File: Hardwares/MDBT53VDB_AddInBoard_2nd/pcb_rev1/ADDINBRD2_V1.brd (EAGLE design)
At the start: 25 x 31 mm, 21 parts, among them CN1 IF_4PIN, CN2 IF_4PIN, CN3 IF_2PIN, CN4 IF_2PIN, Q1 DMP2035UFDF-7, Q2 BC817-40QA, SW1 SKRPACE010, U1 SN74AHC1G00DRLR, U2 REF3325AIRSER, U3 MCP6232T-E/MNY

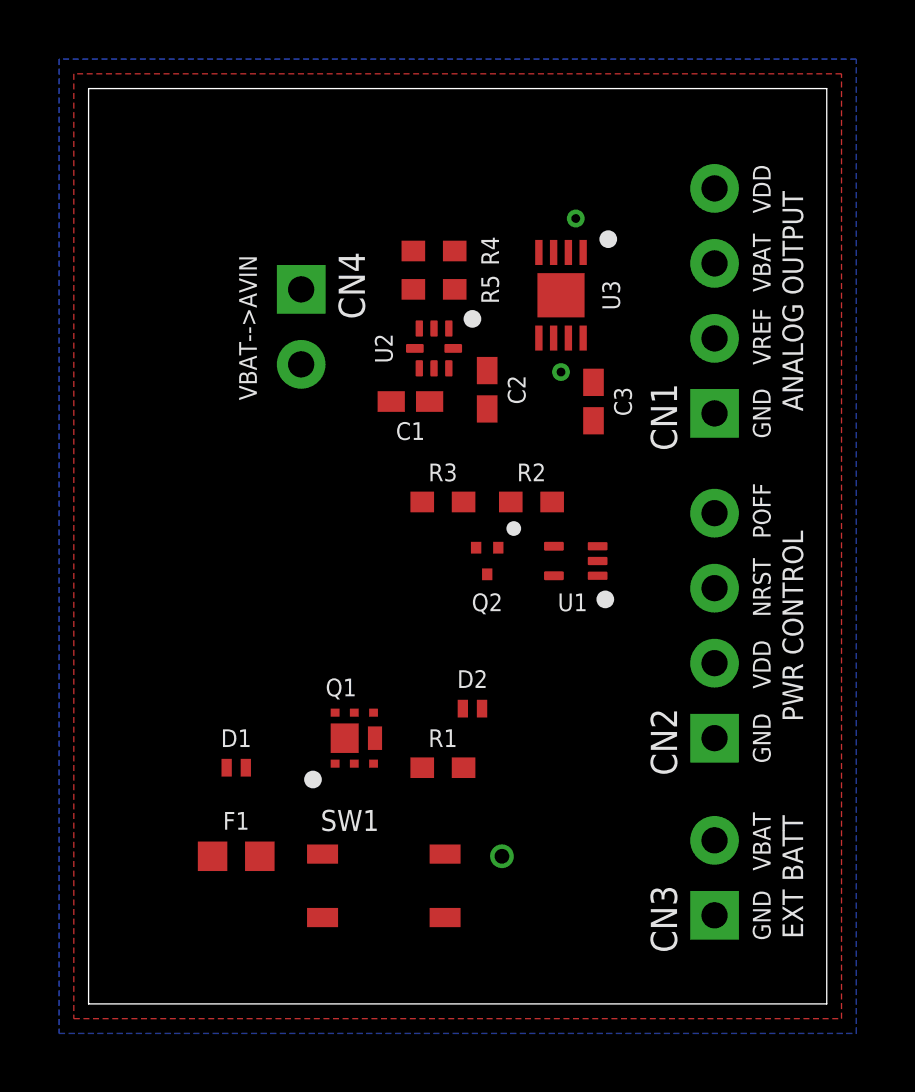
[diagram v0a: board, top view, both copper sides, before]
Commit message: レイアウトを修正
・電源投入回路の部品配置を修正
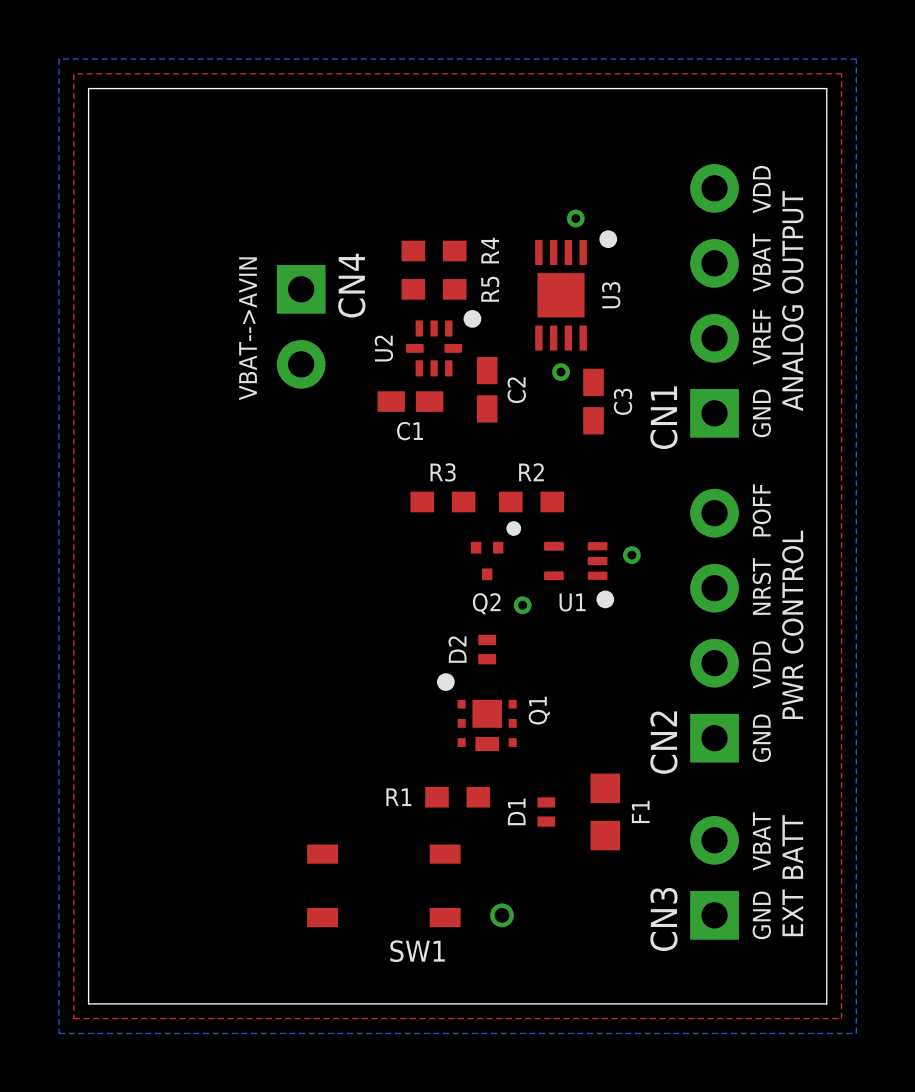
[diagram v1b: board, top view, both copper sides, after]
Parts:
- moved F1 12.6 mm to (17.5, 6.50), turned to 90 degrees
- moved D1 10.6 mm to (15.5, 6.50), turned to 90 degrees
- moved Q1 4.53 mm to (13.5, 9.50), turned to 270 degrees
- moved D2 2.06 mm to (13.5, 12.0), turned to 90 degrees
- moved R1 1.12 mm to (12.5, 7.00)
- turned SW1 to 180 degrees
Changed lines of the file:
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@@
 </autorouter>
 <elements>
-<element name="F1" library="SMDs" package="FCC16" value="FCC16102ABTP" x="5" y="5"/>
-<element name="D1" library="SMDs" package="DSN1006-2" value="PMEG4010AESBYL" x="5" y="8"/>
-<element name="SW1" library="Parts" package="SKRPACE010" value="SKRPACE010" x="10" y="4"/>
-<element name="R1" library="SMDs" package="R0402N" value="5.1k" x="12" y="8"/>
-<element name="D2" library="SMDs" package="DSN1006-2" value="PMEG4010AESBYL" x="13" y="10"/>
+<element name="F1" library="SMDs" package="FCC16" value="FCC16102ABTP" x="17.5" y="6.5" smashed="yes" rot="R90">
+<attribute name="NAME" x="18.4" y="6.5" size="0.6" layer="25" rot="R90" align="top-center"/>
+<attribute name="VALUE" x="18.4" y="6.5" size="0.6" layer="27" rot="R90" align="top-center"/>
+</element>
+<element name="D1" library="SMDs" package="DSN1006-2" value="PMEG4010AESBYL" x="15.5" y="6.5" rot="R90"/>
+<element name="SW1" library="Parts" package="SKRPACE010" value="SKRPACE010" x="10" y="4" rot="R180"/>
+<element name="R1" library="SMDs" package="R0402N" value="5.1k" x="12.5" y="7" smashed="yes">
+<attribute name="NAME" x="11" y="7" size="0.6" layer="25" align="center-right"/>
+<attribute name="VALUE" x="12.5" y="6.2" size="0.6" layer="27" align="top-center"/>
+</element>
+<element name="D2" library="SMDs" package="DSN1006-2" value="PMEG4010AESBYL" x="13.5" y="12" rot="R90"/>
 <element name="R2" library="SMDs" package="R0402N" value="5.1k" x="15" y="17" smashed="yes" rot="R180">
 <attribute name="NAME" x="15" y="17.7" size="0.6" layer="25" align="bottom-center"/>
@@
 <attribute name="VALUE" x="17.8" y="20.4" size="0.6" layer="27" rot="R90" align="top-center"/>
 </element>
-<element name="Q1" library="SMDs" package="U-DFN2020-6" value="DMP2035UFDF-7" x="9" y="9"/>
+<element name="Q1" library="SMDs" package="U-DFN2020-6" value="DMP2035UFDF-7" x="13.5" y="9.5" rot="R270"/>
 <element name="Q2" library="SMDs" package="DFN1010D-3" value="BC817-40QA" x="13.5" y="15" smashed="yes">
 <attribute name="VALUE" x="13" y="13.5" size="0.6" layer="27"/>
@@
 <contactref element="SW1" pad="1"/>
 <contactref element="SW1" pad="2"/>
-<via x="14" y="5" extent="1-16" drill="0.5"/>
+<via x="14" y="3" extent="1-16" drill="0.5"/>
 <contactref element="U2" pad="4"/>
 <contactref element="C1" pad="2"/>
@@
 <contactref element="Q1" pad="EXP2"/>
 <contactref element="Q1" pad="4"/>
-<wire x1="9.7" y1="9" x2="12.7" y2="8" width="0" layer="19" extent="1-1"/>
-<wire x1="9.65" y1="9.863" x2="9.7" y2="9" width="0" layer="19" extent="1-1"/>
-<wire x1="5.325" y1="8" x2="9.7" y2="9" width="0" layer="19" extent="1-1"/>
-<wire x1="5.8" y1="5" x2="5.325" y2="8" width="0" layer="19" extent="1-1"/>
+<wire x1="15.5" y1="6.825" x2="17.5" y2="7.3" width="0" layer="19" extent="1-1"/>
+<wire x1="14.363" y1="8.85" x2="15.5" y2="6.825" width="0" layer="19" extent="1-1"/>
+<wire x1="13.5" y1="8.8" x2="14.363" y2="8.85" width="0" layer="19" extent="1-1"/>
+<wire x1="13.2" y1="7" x2="13.5" y2="8.8" width="0" layer="19" extent="1-1"/>
 </signal>
 <signal name="PWR_G">
@@
 <contactref element="Q2" pad="3"/>
 <contactref element="Q1" pad="3"/>
-<wire x1="11.3" y1="8" x2="13.5" y2="14.55" width="0" layer="19" extent="1-1"/>
-<wire x1="9.65" y1="8.137" x2="11.3" y2="8" width="0" layer="19" extent="1-1"/>
-<wire x1="12.075" y1="2.925" x2="11.3" y2="8" width="0" layer="19" extent="1-1"/>
-<wire x1="7.925" y1="2.925" x2="12.075" y2="2.925" width="0" layer="19" extent="1-1"/>
+<wire x1="12.637" y1="8.85" x2="13.5" y2="14.55" width="0" layer="19" extent="1-1"/>
+<wire x1="11.8" y1="7" x2="12.637" y2="8.85" width="0" layer="19" extent="1-1"/>
+<wire x1="12.075" y1="5.075" x2="11.8" y2="7" width="0" layer="19" extent="1-1"/>
+<wire x1="7.925" y1="5.075" x2="12.075" y2="5.075" width="0" layer="19" extent="1-1"/>
 </signal>
 <signal name="VIN">
@@
 <contactref element="CN2" pad="2"/>
 <contactref element="CN4" pad="2"/>
+<via x="14.7" y="13.5" extent="1-16" drill="0.3"/>
 <wire x1="15.76" y1="14.5" x2="21.2" y2="11.54" width="0" layer="19" extent="1-1"/>
-<wire x1="13.325" y1="10" x2="15.76" y2="14.5" width="0" layer="19" extent="1-1"/>
-<wire x1="7.2" y1="21.66" x2="15.76" y2="14.5" width="0" layer="19" extent="1-1"/>
+<wire x1="14.7" y1="13.5" x2="15.76" y2="14.5" width="0" layer="19" extent="1-1"/>
+<wire x1="13.5" y1="12.325" x2="14.7" y2="13.5" width="0" layer="19" extent="1-1"/>
+<wire x1="7.2" y1="21.66" x2="14.7" y2="13.5" width="0" layer="19" extent="1-1"/>
 </signal>
 <signal name="EXT_BAT">
 <contactref element="F1" pad="1"/>
 <contactref element="CN3" pad="2"/>
-<wire x1="4.2" y1="5" x2="21.2" y2="5.54" width="0" layer="19" extent="1-1"/>
+<wire x1="17.5" y1="5.7" x2="21.2" y2="5.54" width="0" layer="19" extent="1-1"/>
 </signal>
 <signal name="N$5">
@@
 <contactref element="Q1" pad="2"/>
 <contactref element="D2" pad="1"/>
-<wire x1="9" y1="9.863" x2="12.675" y2="10" width="0" layer="19" extent="1-1"/>
-<wire x1="8.35" y1="9.863" x2="9" y2="9.863" width="0" layer="19" extent="1-1"/>
-<wire x1="8.675" y1="9" x2="9" y2="9.863" width="0" layer="19" extent="1-1"/>
-<wire x1="8.35" y1="8.137" x2="8.675" y2="9" width="0" layer="19" extent="1-1"/>
-<wire x1="9" y1="8.137" x2="8.35" y2="8.137" width="0" layer="19" extent="1-1"/>
+<wire x1="14.363" y1="10.15" x2="13.5" y2="11.675" width="0" layer="19" extent="1-1"/>
+<wire x1="14.363" y1="9.5" x2="14.363" y2="10.15" width="0" layer="19" extent="1-1"/>
+<wire x1="13.5" y1="9.825" x2="14.363" y2="10.15" width="0" layer="19" extent="1-1"/>
+<wire x1="12.637" y1="10.15" x2="13.5" y2="9.825" width="0" layer="19" extent="1-1"/>
+<wire x1="12.637" y1="9.5" x2="12.637" y2="10.15" width="0" layer="19" extent="1-1"/>
 </signal>
 <signal name="N$3">
@@
 <contactref element="U1" pad="2"/>
 <contactref element="CN2" pad="3"/>
-<wire x1="17.24" y1="15" x2="21.2" y2="14.08" width="0" layer="19" extent="1-1"/>
+<via x="18.4" y="15.2" extent="1-16" drill="0.3"/>
+<wire x1="18.4" y1="15.2" x2="21.2" y2="14.08" width="0" layer="19" extent="1-1"/>
+<wire x1="17.24" y1="15" x2="18.4" y2="15.2" width="0" layer="19" extent="1-1"/>
 </signal>
 <signal name="PWR_OFF">

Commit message: レイアウトを修正
・バイパスコンデンサーの位置を調整
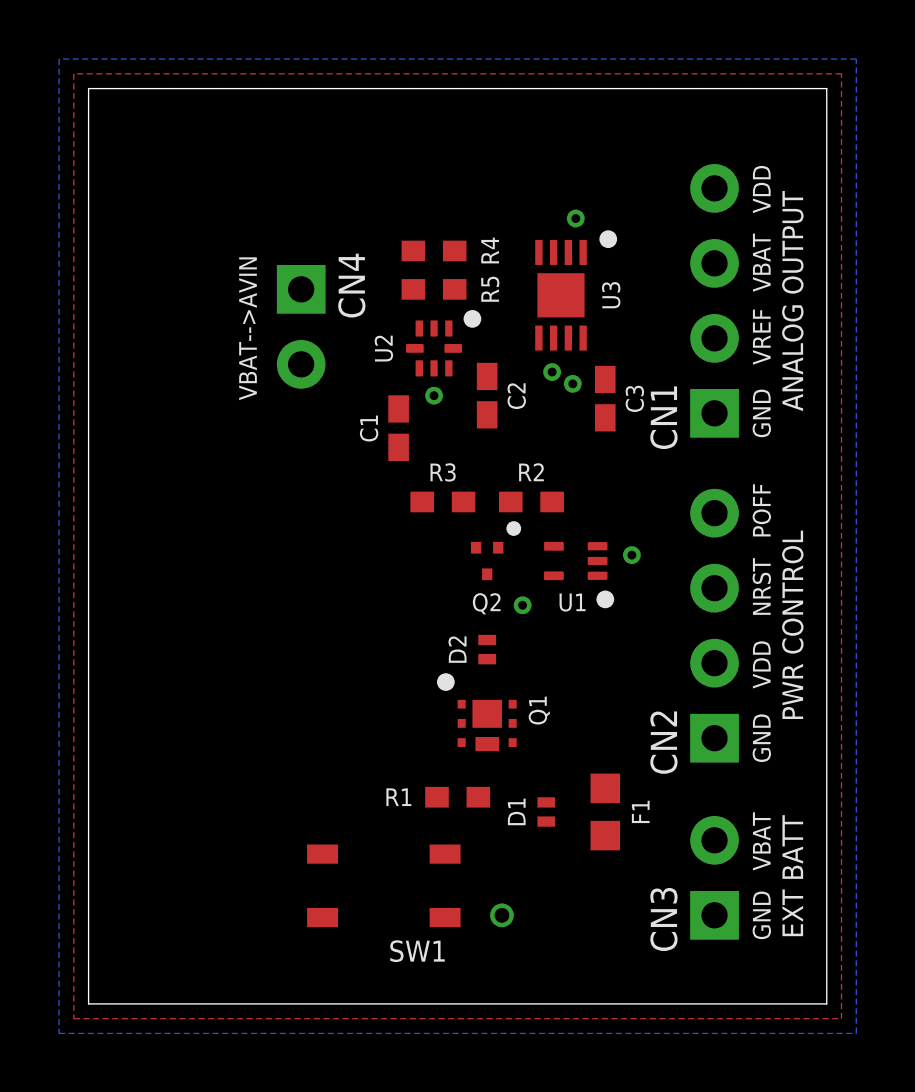
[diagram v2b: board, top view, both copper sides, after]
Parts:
- moved C1 0.98 mm to (10.5, 19.5), turned to 270 degrees
- moved C3 0.41 mm to (17.5, 20.5), turned to 270 degrees
- moved C2 0.20 mm to (13.5, 20.6)
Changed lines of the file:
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@@
 <attribute name="NAME" x="10.3" y="22.2" size="0.6" layer="25" rot="R90" align="bottom-center"/>
 </element>
-<element name="C1" library="SMDs" package="C0402" value="1uF" x="10.9" y="20.4" rot="R180"/>
-<element name="C2" library="SMDs" package="C0402" value="1uF" x="13.5" y="20.8" smashed="yes" rot="R270">
-<attribute name="NAME" x="14.2" y="20.8" size="0.6" layer="25" rot="R270" align="bottom-center"/>
-<attribute name="VALUE" x="12.8" y="20.8" size="0.6" layer="27" rot="R270" align="top-center"/>
+<element name="C1" library="SMDs" package="C0402" value="1uF" x="10.5" y="19.5" smashed="yes" rot="R270">
+<attribute name="NAME" x="9.8" y="19.5" size="0.6" layer="25" rot="R90" align="bottom-center"/>
+<attribute name="VALUE" x="9.8" y="19.5" size="0.6" layer="27" rot="R270" align="top-center"/>
+</element>
+<element name="C2" library="SMDs" package="C0402" value="1uF" x="13.5" y="20.6" smashed="yes" rot="R270">
+<attribute name="NAME" x="14.2" y="20.6" size="0.6" layer="25" rot="R270" align="bottom-center"/>
+<attribute name="VALUE" x="12.8" y="20.6" size="0.6" layer="27" rot="R270" align="top-center"/>
 </element>
 <element name="R4" library="SMDs" package="R0402N" value="5.1k" x="11.7" y="24.2" smashed="yes">
@@
 <attribute name="VALUE" x="11.7" y="26.3" size="0.6" layer="27" rot="R180" align="top-center"/>
 </element>
-<element name="C3" library="SMDs" package="C0402" value="0.1uF" x="17.1" y="20.4" smashed="yes" rot="R90">
-<attribute name="NAME" x="17.8" y="20.4" size="0.6" layer="25" rot="R90" align="top-center"/>
-<attribute name="VALUE" x="17.8" y="20.4" size="0.6" layer="27" rot="R90" align="top-center"/>
+<element name="C3" library="SMDs" package="C0402" value="0.1uF" x="17.5" y="20.5" smashed="yes" rot="R270">
+<attribute name="NAME" x="18.2" y="20.5" size="0.6" layer="25" rot="R90" align="top-center"/>
+<attribute name="VALUE" x="16.8" y="20.5" size="0.6" layer="27" rot="R270" align="top-center"/>
 </element>
 <element name="Q1" library="SMDs" package="U-DFN2020-6" value="DMP2035UFDF-7" x="13.5" y="9.5" rot="R270"/>
@@
 <contactref element="CN2" pad="1"/>
 <wire x1="16" y1="24" x2="15.25" y2="25.45" width="0" layer="19" extent="1-1"/>
-<wire x1="11.05" y1="22.2" x2="10.25" y2="20.4" width="0" layer="19" extent="1-1"/>
+<wire x1="11.05" y1="22.2" x2="11" y2="25.5" width="0" layer="19" extent="1-1"/>
 <wire x1="17.24" y1="15.5" x2="13.125" y2="15.45" width="0" layer="19" extent="1-1"/>
 </signal>
@@
 <contactref element="C2" pad="1"/>
 <contactref element="U3" pad="5"/>
-<wire x1="13.5" y1="21.45" x2="15.25" y2="22.55" width="0" layer="19" extent="1-1"/>
-<wire x1="12.35" y1="22.2" x2="13.5" y2="21.45" width="0" layer="19" extent="1-1"/>
+<wire x1="13.5" y1="21.25" x2="15.25" y2="22.55" width="0" layer="19" extent="1-1"/>
+<wire x1="12.35" y1="22.2" x2="13.5" y2="21.25" width="0" layer="19" extent="1-1"/>
 </signal>
 <signal name="AVBAT_IN">
@@
 <contactref element="U3" pad="6"/>
 <contactref element="CN1" pad="2"/>
-<via x="16" y="21.4" extent="1-16" drill="0.3"/>
+<via x="15.7" y="21.4" extent="1-16" drill="0.3"/>
 <wire x1="16.25" y1="22.55" x2="21.2" y2="22.54" width="0" layer="19" extent="1-1"/>
 <wire x1="15.75" y1="22.55" x2="16.25" y2="22.55" width="0" layer="19" extent="1-1"/>
-<wire x1="16" y1="21.4" x2="16.25" y2="22.55" width="0" layer="19" extent="1-1"/>
+<wire x1="15.7" y1="21.4" x2="15.75" y2="22.55" width="0" layer="19" extent="1-1"/>
 </signal>
 <signal name="AVIN">
@@
 <contactref element="U3" pad="8"/>
 <contactref element="CN4" pad="1"/>
+<via x="16.4" y="21" extent="1-16" drill="0.3"/>
+<via x="11.7" y="20.6" extent="1-16" drill="0.3"/>
 <wire x1="16.75" y1="22.55" x2="21.2" y2="27.62" width="0" layer="19" extent="1-1"/>
-<wire x1="17.1" y1="19.75" x2="16.75" y2="22.55" width="0" layer="19" extent="1-1"/>
-<wire x1="11.55" y1="20.4" x2="17.1" y2="19.75" width="0" layer="19" extent="1-1"/>
-<wire x1="11.2" y1="21.525" x2="11.55" y2="20.4" width="0" layer="19" extent="1-1"/>
+<wire x1="17.5" y1="21.15" x2="16.75" y2="22.55" width="0" layer="19" extent="1-1"/>
+<wire x1="16.4" y1="21" x2="17.5" y2="21.15" width="0" layer="19" extent="1-1"/>
+<wire x1="11.7" y1="20.6" x2="16.4" y2="21" width="0" layer="19" extent="1-1"/>
+<wire x1="11.2" y1="21.525" x2="11.7" y2="20.6" width="0" layer="19" extent="1-1"/>
+<wire x1="10.5" y1="20.15" x2="11.7" y2="20.6" width="0" layer="19" extent="1-1"/>
 <wire x1="11" y1="24.2" x2="11.2" y2="21.525" width="0" layer="19" extent="1-1"/>
 <wire x1="7.2" y1="24.2" x2="11" y2="24.2" width="0" layer="19" extent="1-1"/>

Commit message: レイアウトを修正
・部品配置を変更
・シルク文言を修正
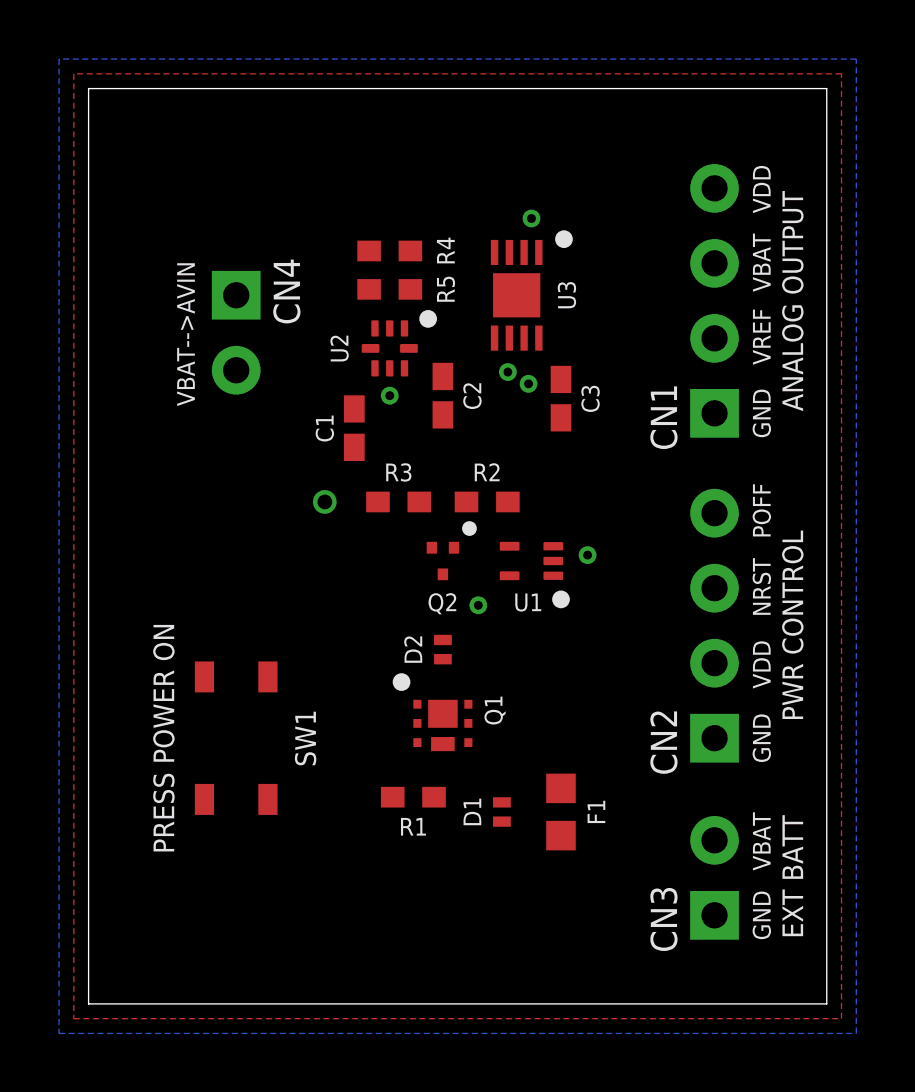
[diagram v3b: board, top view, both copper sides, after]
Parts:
- moved SW1 7.07 mm to (5.00, 9.00), turned to 90 degrees
- moved CN4 2.21 mm to (5.00, 24.0)
- moved C1 1.50 mm to (9.00, 19.5)
- moved C2 1.50 mm to (12.0, 20.6)
- moved C3 1.50 mm to (16.0, 20.5)
- moved D1 1.50 mm to (14.0, 6.50)
- moved D2 1.50 mm to (12.0, 12.0)
- moved F1 1.50 mm to (16.0, 6.50)
- moved Q1 1.50 mm to (12.0, 9.50)
- moved Q2 1.50 mm to (12.0, 15.0)
- moved R1 1.50 mm to (11.0, 7.00)
- moved R2 1.50 mm to (13.5, 17.0)
- moved R3 1.50 mm to (10.5, 17.0)
- moved R4 1.50 mm to (10.2, 24.2)
- moved R5 1.50 mm to (10.2, 25.5)
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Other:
- board text added: "PRESS POWER ON"
